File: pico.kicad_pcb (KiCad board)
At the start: 2 copper layers, 103 x 101.2 mm, 61 parts, among them J101 Programming, J102 ???, J103 XT60, J201 MR30, Q101 IRFS7434TRL7PP, Q201 SQJ142EP-T1_GE3, Q202 SQJ142EP-T1_GE3, Q203 SQJ142EP-T1_GE3, Q204 SQJ142EP-T1_GE3, Q205 SQJ142EP-T1_GE3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

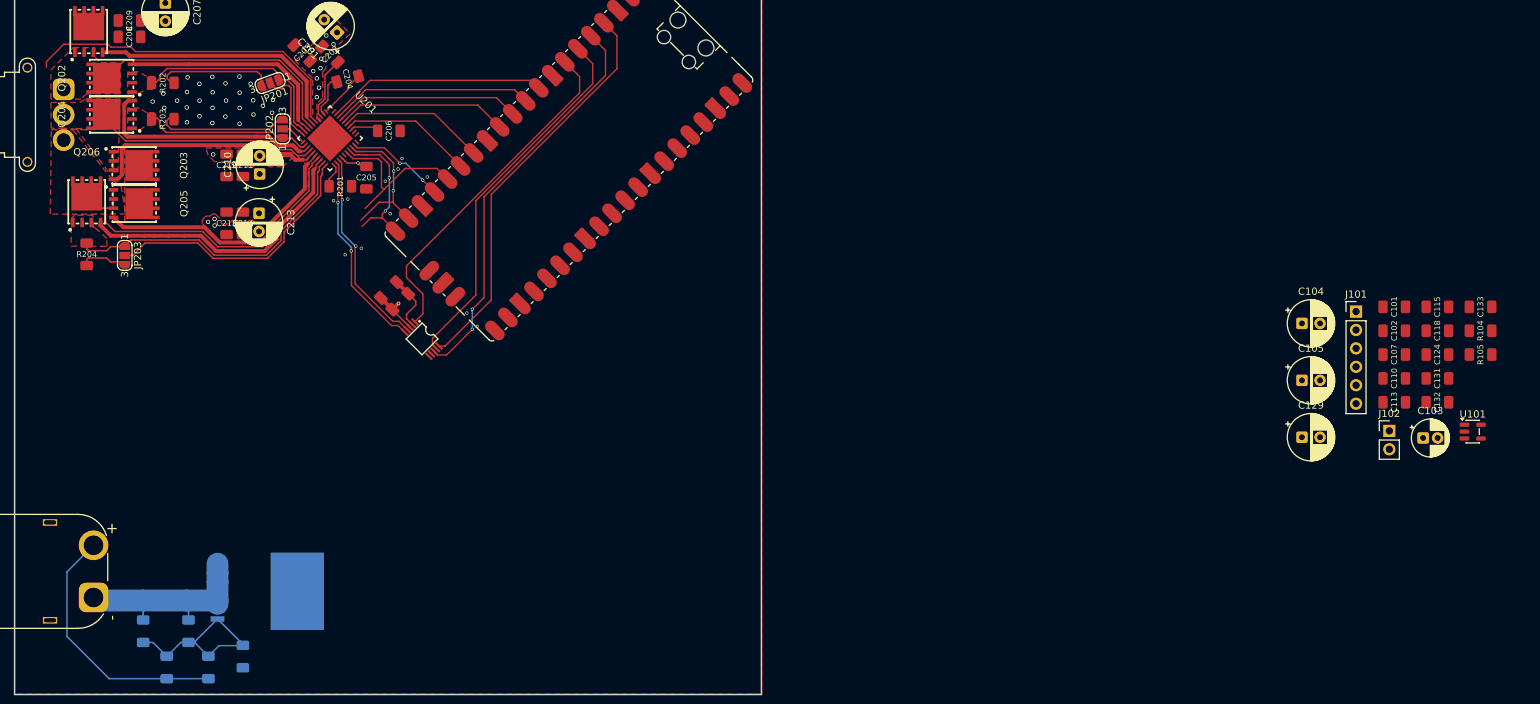
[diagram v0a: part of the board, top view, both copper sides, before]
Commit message: progress on pcb todo:encoders
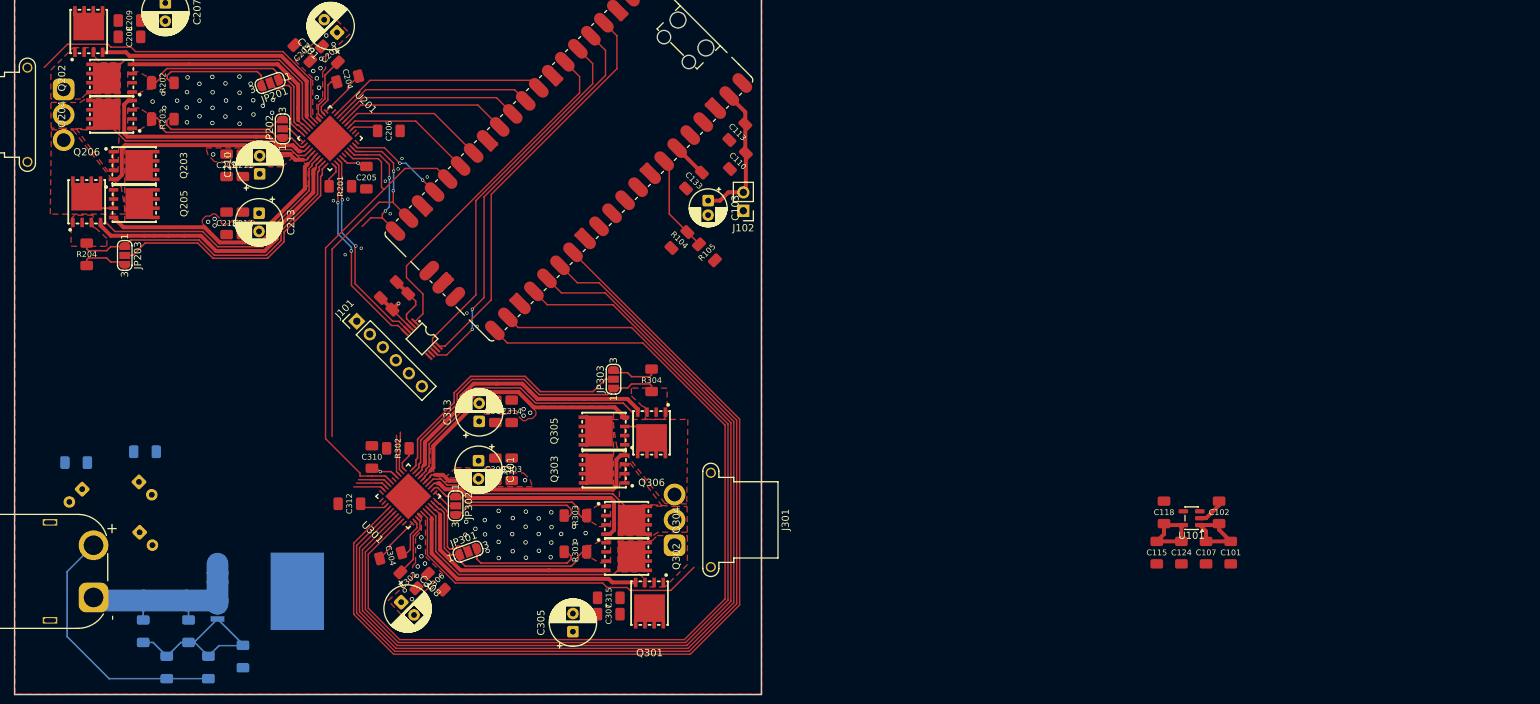
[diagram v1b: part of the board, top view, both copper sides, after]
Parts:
- added C301: 47u, Capacitor_THT:CP_Radial_D6.3mm_P2.50mm, F.Cu at (74.5, 129.2)
- added C302: 1u, COMPONENTS:1206_Resistor, F.Cu at (64.8, 145.7)
- added C303: 100n, COMPONENTS:1206_Resistor, F.Cu at (79.1, 130.4)
- added C304: 47n, COMPONENTS:1206_Resistor, F.Cu at (62.4, 142.3)
- added C305: 47u low ESR, Capacitor_THT:CP_Radial_D6.3mm_P2.50mm, F.Cu at (87.5, 152.8)
- added C306: 10u, COMPONENTS:1206_Resistor, F.Cu at (68.6, 145.9)
- added C307: 1u, COMPONENTS:1206_Resistor, F.Cu at (92.5, 150.4)
- added C308: 47u low ESR, Capacitor_THT:CP_Radial_D6.3mm_P2.50mm, F.Cu at (63.8, 148.7)
- added C309: 10u, COMPONENTS:1206_Resistor, F.Cu at (76.8, 130.4)
- added C310: 100n, COMPONENTS:1206_Resistor, F.Cu at (59.8, 128.7)
- added C311: 1u, COMPONENTS:1206_Resistor, F.Cu at (76.8, 122.4)
- added C312: 1u, COMPONENTS:1206_Resistor, F.Cu at (56.7, 135.2)
- added C313: 47u low ESR, Capacitor_THT:CP_Radial_D6.3mm_P2.50mm, F.Cu at (74.6, 123.8)
- added C314: 10u, COMPONENTS:1206_Resistor, F.Cu at (79.1, 122.4)
- added C315: 1u, COMPONENTS:1206_Resistor, F.Cu at (92.5, 148.2)
- added J301: MR30, Connector_AMASS:AMASS_MR30PW-FB_1x03_P3.50mm_Horizontal, F.Cu at (101.5, 140.9)
- added JP301: SolderJumper_3_Open, Jumper:SolderJumper-3_P1.3mm_Open_RoundedPad1.0x1.5mm_NumberLabels, F.Cu at (73.1, 141.8)
- added JP302: SolderJumper_3_Open, Jumper:SolderJumper-3_P1.3mm_Open_RoundedPad1.0x1.5mm_NumberLabels, F.Cu at (71.3, 135.5)
- added JP303: SolderJumper_3_Open, Jumper:SolderJumper-3_P1.3mm_Open_RoundedPad1.0x1.5mm_NumberLabels, F.Cu at (93.1, 118.0)
- added Q301: SQJ142EP-T1_GE3, JLCPCB_Transistors_Thyristors:POWERPAK-SO-8_L5.9-W4.9-P1.27-BL, F.Cu at (98.1, 148.9)
- added Q302: SQJ142EP-T1_GE3, JLCPCB_Transistors_Thyristors:POWERPAK-SO-8_L5.9-W4.9-P1.27-BL, F.Cu at (94.9, 142.4)
- added Q303: SQJ142EP-T1_GE3, JLCPCB_Transistors_Thyristors:POWERPAK-SO-8_L5.9-W4.9-P1.27-BL, F.Cu at (91.8, 130.4)
- added Q304: SQJ142EP-T1_GE3, JLCPCB_Transistors_Thyristors:POWERPAK-SO-8_L5.9-W4.9-P1.27-BL, F.Cu at (94.9, 137.4)
- added Q305: SQJ142EP-T1_GE3, JLCPCB_Transistors_Thyristors:POWERPAK-SO-8_L5.9-W4.9-P1.27-BL, F.Cu at (91.8, 125.1)
- added Q306: SQJ142EP-T1_GE3, JLCPCB_Transistors_Thyristors:POWERPAK-SO-8_L5.9-W4.9-P1.27-BL, F.Cu at (98.4, 125.4)
- added R301: 2m, COMPONENTS:1206_Resistor, F.Cu at (87.9, 141.8)
- added R302: 100k, COMPONENTS:1206_Resistor, F.Cu at (63.4, 127.5)
- added R303: 2m, COMPONENTS:1206_Resistor, F.Cu at (87.9, 136.8)
- added R304: 2m, COMPONENTS:1206_Resistor, F.Cu at (98.4, 118.2)
- added U301: DRV8323SRTAT, JLCPCB_Power_Supply_Chip:WQFN-40_L6.0-W6.0-P0.50-TL-EP4.5, F.Cu at (64.8, 134.1)
- C104, C105, C129, C131, C132: moved to B.Cu
- U101: value TPS7A2050PDBVR -> TPS7A2033PDBVR
- moved C132 187.9 mm to (19.0, 129.5), turned to 180 degrees
- moved C131 178.5 mm to (28.5, 128.0)
- moved C104 169.8 mm to (19.8, 133.2), turned to -135 degrees
- moved C105 161.0 mm to (27.7, 132.2), turned to -45 degrees
- moved C129 160.8 mm to (27.8, 139.1), turned to -45 degrees
- moved J101 137.8 mm to (57.7, 110.0), turned to 45 degrees
- moved R104 111.2 mm to (102.2, 98.8), turned to 45 degrees
- moved C133 109.9 mm to (104.2, 90.6), turned to -135 degrees
- moved R105 107.6 mm to (106.0, 100.5), turned to -45 degrees
- moved C103 103.9 mm to (106.2, 93.4), turned to -90 degrees
- moved C113 98.0 mm to (110.2, 83.9), turned to -135 degrees
- moved C110 95.4 mm to (110.3, 87.9), turned to -135 degrees
- moved J102 94.1 mm to (111.0, 94.8), turned to 180 degrees
- moved C115 51.4 mm to (168.0, 141.9), turned to -90 degrees
- moved C118 45.3 mm to (169.0, 136.4), turned to 90 degrees
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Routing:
- net PWM_B_X_H: track 0.00 -> 133.2 mm
- net PWM_B_X_L: track 0.00 -> 132.0 mm
- net PWM_B_Y_H: track 0.00 -> 130.9 mm
- net PWM_B_Y_L: track 0.00 -> 129.7 mm
- net PWM_B_Z_H: track 0.00 -> 129.6 mm
- net PWM_B_Z_L: track 0.00 -> 128.5 mm
- net /MotorDriver1/Z: track 0.00 -> 47.4 mm
- net GND: track 49.1 -> 95.2 mm, vias 50 -> 88
- net +BATT: track 82.4 -> 128.4 mm, vias 9 -> 18
- net SPI0_RX: track 23.6 -> 69.5 mm
- net /MotorDriver1/Z_S_H: track 0.00 -> 43.2 mm
- net /MotorDriver1/Z_L: track 0.00 -> 40.2 mm
- net /MotorDriver1/Z_S_L: track 0.00 -> 37.5 mm
- net /MotorDriver1/Z_H: track 0.00 -> 37.0 mm
- net /MotorDriver1/X_H: track 0.00 -> 36.1 mm
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- added copper zone on F.Cu, net /MotorDriver1/X
- added copper zone on F.Cu, net /MotorDriver1/X_S_H
- added copper zone on F.Cu, net /MotorDriver1/Y
- added copper zone on F.Cu, net /MotorDriver1/Y_S_H
- added copper zone on F.Cu, net /MotorDriver1/Z
- added copper zone on F.Cu, net /MotorDriver1/Z_S_H

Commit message: added m3 mounting holes
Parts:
- added H101: MountingHole, MountingHole:MountingHole_3.2mm_M3, F.Cu at (12.8, 62.5)
- added H102: MountingHole, MountingHole:MountingHole_3.2mm_M3, F.Cu at (111.3, 62.5)
- added H103: MountingHole, MountingHole:MountingHole_3.2mm_M3, F.Cu at (111.3, 159.3)
- added H104: MountingHole, MountingHole:MountingHole_3.2mm_M3, F.Cu at (12.8, 159.3)
- moved C118 51.6 mm to (125.2, 109.3)
- moved C101 51.6 mm to (134.4, 114.8)
- moved C107 51.6 mm to (131.0, 114.8)
- moved U101 51.6 mm to (129.0, 110.1)
- moved C115 51.6 mm to (124.2, 114.8)
- moved C124 51.6 mm to (127.6, 114.8)
- moved C102 51.6 mm to (132.8, 109.2)

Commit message: ewdwad
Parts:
- added J104: Conn_01x03, Connector_JST:JST_EH_B3B-EH-A_1x03_P2.50mm_Vertical, F.Cu at (83.5, 67.8)
- moved H104 3.36 mm to (15.0, 156.8)
- moved H103 2.66 mm to (109.5, 157.3)
- moved H101 2.47 mm to (14.5, 64.3)
- moved H102 2.47 mm to (109.5, 64.3)
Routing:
- net ENable: track 0.00 -> 30.5 mm
- net UartRX: track 0.00 -> 12.1 mm
- net UartTX: track 0.00 -> 11.9 mm
- net PWM_B_Z_L: track 128.5 -> 130.9 mm
- net PWM_B_Z_H: track 129.6 -> 132.1 mm
- net PWM_B_X_L: track 132.0 -> 134.5 mm
- net PWM_B_Y_L: track 129.7 -> 132.2 mm
- net PWM_B_Y_H: track 130.9 -> 133.3 mm
- net PWM_B_X_H: track 133.2 -> 135.6 mm

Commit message: wdawdawd
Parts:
- moved J101 17.2 mm to (46.6, 123.1), turned to 180 degrees
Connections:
- U106 pad 6: ADC2+ -> ADC3+
- U106 pad 7: ADC3+ -> ADC2+
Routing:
- net SPI0_TX: track 24.5 -> 61.6 mm
- net SPI0_RX: track 69.5 -> 34.4 mm
- net CS_ENCODER_A: track 0.00 -> 22.7 mm, vias 0 -> 1
- net CS_ENCODER_B: track 0.00 -> 20.6 mm, vias 0 -> 1
- net CS_DRV_B: track 4.78 -> 20.0 mm, vias 0 -> 1
- net SPI0_CLK: track 56.5 -> 64.3 mm
- net ADC3+: track 5.57 -> 4.05 mm
- net ADC2+: track 5.69 -> 4.36 mm
- net SPI1_CS: track 48.0 -> 48.9 mm
- net PWM_B_X_H: track 135.6 -> 136.1 mm

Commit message: why every commit needs a message
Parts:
- added Q102: BSS138, Package_TO_SOT_SMD:SOT-23, F.Cu at (34.3, 112.8)
- added R102: 100, COMPONENTS:1206_Resistor, F.Cu at (34.8, 108.9)
- moved C305 0.34 mm to (87.5, 152.5)
- moved C214 0.13 mm to (42.0, 96.4)
- moved C215 0.12 mm to (39.8, 96.4)
- moved C314 0.06 mm to (79.1, 122.5)
- moved C311 0.06 mm to (76.8, 122.5)
- moved C313 0.05 mm to (74.6, 123.8)
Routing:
- net PWM_B_Z_L: track 130.9 -> 132.2 mm
- net PWM_B_Z_H: track 132.2 -> 133.4 mm
- net PWM_B_Y_L: track 132.4 -> 133.6 mm
- net PWM_B_X_L: track 134.9 -> 136.1 mm
- net PWM_B_Y_H: track 133.6 -> 134.9 mm
- net PWM_B_X_H: track 136.1 -> 137.4 mm

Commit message: Good progress
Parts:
- removed C117: 1u, COMPONENTS:1206_Resistor
- removed C122: DNP, COMPONENTS:1206_Resistor
- removed C123: 100n, COMPONENTS:1206_Resistor
- removed J201, J301: MR30, Connector_AMASS:AMASS_MR30PW-FB_1x03_P3.50mm_Horizontal
- removed R114: 2Meg, COMPONENTS:1206_Resistor
- added C106: 2200u, Capacitor_THT:CP_Radial_D18.0mm_P7.50mm, F.Cu at (47.0, 140.5)
- added H201: MountingHole_Pad, Connector_Wire:SolderWire-2sqmm_1x01_D2mm_OD3.9mm, F.Cu at (14.5, 75.3)
- added H202: MountingHole_Pad, Connector_Wire:SolderWire-2sqmm_1x01_D2mm_OD3.9mm, F.Cu at (14.5, 83.3)
- added H203: MountingHole_Pad, Connector_Wire:SolderWire-2sqmm_1x01_D2mm_OD3.9mm, F.Cu at (14.5, 91.8)
- added H301: MountingHole_Pad, Connector_Wire:SolderWire-2sqmm_1x01_D2mm_OD3.9mm, F.Cu at (104.8, 143.0)
- added H302: MountingHole_Pad, Connector_Wire:SolderWire-2sqmm_1x01_D2mm_OD3.9mm, F.Cu at (104.8, 135.3)
- added H303: MountingHole_Pad, Connector_Wire:SolderWire-2sqmm_1x01_D2mm_OD3.9mm, F.Cu at (104.8, 127.3)
- added Q103: AGM30P100D, EasyEDA_Lib:TO-252-3_L6.6-W6.1-P4.57-LS9.9-BR-CW, B.Cu at (34.3, 133.0)
- added Q104: AGM30P100D, EasyEDA_Lib:TO-252-3_L6.6-W6.1-P4.57-LS9.9-BR-CW, B.Cu at (34.3, 125.8)
- added Q105: AGM30P100D, EasyEDA_Lib:TO-252-3_L6.6-W6.1-P4.57-LS9.9-BR-CW, B.Cu at (34.3, 118.5)
- added Q106: AGM30P100D, EasyEDA_Lib:TO-252-3_L6.6-W6.1-P4.57-LS9.9-BR-CW, B.Cu at (34.3, 111.3)
- added R103: 100, COMPONENTS:1206_Resistor, B.Cu at (39.3, 148.3)
- added R106: 100, COMPONENTS:1206_Resistor, B.Cu at (36.8, 148.3)
- added R107: 100, COMPONENTS:1206_Resistor, B.Cu at (34.0, 148.3)
- added R108: 5k, COMPONENTS:1206_Resistor, F.Cu at (24.8, 116.3)
- C104, C105, C129: moved to F.Cu
- Q101: value IRFS7434TRL7PP -> AGM30P100D; footprint JLCPCB_Transistors:D2PAK-7_L10.6-W9.6-P1.27-LS15.9-BR -> EasyEDA_Lib:TO-252-3_L6.6-W6.1-P4.57-LS9.9-BR-CW
- R101: value 100k -> 100
- R102: moved to B.Cu
- moved J101 120.9 mm to (162.0, 87.2)
- moved C124 70.0 mm to (71.8, 72.4)
- moved C115 70.0 mm to (68.4, 72.4)
- moved C102 70.0 mm to (77.0, 66.9)
- moved U101 70.0 mm to (73.2, 67.7)
- moved C118 70.0 mm to (69.4, 66.9)
- moved C107 70.0 mm to (75.2, 72.4)
- moved C101 70.0 mm to (78.6, 72.4)
- moved C104 40.0 mm to (-20.2, 133.2), turned to -45 degrees
- moved C105 40.0 mm to (-12.4, 132.2), turned to -135 degrees
- moved C129 40.0 mm to (-12.3, 139.1), turned to -135 degrees
- moved C131 40.0 mm to (-11.5, 128.0)
- moved C132 40.0 mm to (-21.0, 129.5)
- moved R102 40.0 mm to (41.8, 148.3), turned to 90 degrees
- moved J103 18.4 mm to (21.4, 129.7)
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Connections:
- J103 pad 1: Net-(J103-Pin_1) -> GND
- J103 pad 2: +BATT -> /IN
- Q101 pad 2: Net-(J103-Pin_1) -> +BATT
- Q101 pad 3: Net-(J103-Pin_1) -> /IN
- Q102 pad 1: ENableBATT -> ENable
- Q102 pad 2: Net-(Q101-G) -> GND
- Q102 pad 3: +BATT -> Net-(Q101-G)
- R101 pad 1: +BATT -> /IN
- R101 pad 2: Net-(Q101-G) -> +BATT
- R102 pad 1: Net-(J103-Pin_1) -> /IN
- R102 pad 2: GND -> +BATT
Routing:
- net +LDO: track 32.0 -> 144.2 mm, vias 2 -> 7
- net +BATT: track 128.4 -> 37.5 mm
- net ENable: track 30.8 -> 74.3 mm, vias 0 -> 2
- net +5VP: track 31.6 -> 70.3 mm, vias 0 -> 2
- net /IN: track 0.00 -> 31.3 mm
- net Net-(J103-Pin_1): track 28.3 -> 0.00 mm
- net Net-(Q101-G): track 27.1 -> 44.7 mm, vias 0 -> 5
- net SPI0_RX: track 34.0 -> 21.4 mm
- net Net-(U201-CPL): track 6.72 -> 8.79 mm
- net GND: track 95.2 -> 95.8 mm, vias 88 -> 135
- added copper zone on F.Cu, net +5VP
- added copper zone on B.Cu, net +BATT
- added copper zone on F.Cu, net +LDO
- added copper zone on B.Cu, net /IN

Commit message: done?
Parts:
- removed C103: 22u, Capacitor_THT:CP_Radial_D5.0mm_P2.00mm
- removed C131: 10u, COMPONENTS:1206_Resistor
- removed C132: 1u, COMPONENTS:1206_Resistor
- removed H101, H102, H103, H104: MountingHole, MountingHole:MountingHole_3.2mm_M3
- removed J102: ???, Connector_PinHeader_2.54mm:PinHeader_1x02_P2.54mm_Vertical
- added H105: MountingHole_Pad, MountingHole:MountingHole_3.2mm_M3_Pad_Via, F.Cu at (14.5, 64.3)
- added H106: MountingHole_Pad, MountingHole:MountingHole_3.2mm_M3_Pad_Via, F.Cu at (109.5, 64.3)
- added H107: MountingHole_Pad, MountingHole:MountingHole_3.2mm_M3_Pad_Via, F.Cu at (109.5, 157.4)
- added H108: MountingHole_Pad, MountingHole:MountingHole_3.2mm_M3_Pad_Via, F.Cu at (14.5, 157.4)
- added J105: Conn_01x03, Connector_JST:JST_XH_B3B-XH-A_1x03_P2.50mm_Vertical, F.Cu at (101.8, 95.7)
- added J106: Conn_01x03, Connector_JST:JST_XH_B3B-XH-A_1x03_P2.50mm_Vertical, F.Cu at (56.2, 110.4)
- added J107: Conn_01x03, Connector_JST:JST_XH_B3B-XH-A_1x03_P2.50mm_Vertical, F.Cu at (95.8, 101.7)
- added J108: Conn_01x03, Connector_JST:JST_XH_B3B-XH-A_1x03_P2.50mm_Vertical, F.Cu at (55.6, 119.7)
- added JP101: SolderJumper_2_Open, Jumper:SolderJumper-2_P1.3mm_Open_RoundedPad1.0x1.5mm, F.Cu at (102.1, 63.1)
- J101: value Programming -> Conn_01x03; footprint Connector_PinHeader_2.54mm:PinHeader_1x06_P2.54mm_Vertical -> Connector_JST:JST_XH_B3B-XH-A_1x03_P2.50mm_Vertical
- J104: footprint Connector_JST:JST_EH_B3B-EH-A_1x03_P2.50mm_Vertical -> Connector_JST:JST_XH_B3B-XH-A_1x03_P2.50mm_Vertical
- moved J101 99.7 mm to (64.1, 68.7), turned to 90 degrees
- moved C104 62.1 mm to (34.1, 103.1), turned to 180 degrees
- moved C129 60.6 mm to (47.7, 130.5), turned to 135 degrees
- moved C105 59.4 mm to (46.4, 123.4), turned to 90 degrees
- moved C101 9.83 mm to (76.6, 62.8), turned to 0 degrees
- moved R104 9.32 mm to (110.9, 95.5), turned to 90 degrees
- moved R105 8.41 mm to (108.4, 92.4), turned to 90 degrees
- moved C115 8.24 mm to (76.6, 73.0), turned to 0 degrees
- moved C102 6.43 mm to (71.1, 64.4), turned to 180 degrees
- moved C107 6.38 mm to (76.6, 66.2), turned to 0 degrees
- moved C124 5.59 mm to (76.6, 69.6), turned to 0 degrees
- moved C118 5.39 mm to (71.1, 72.0), turned to 180 degrees
- moved C133 3.10 mm to (106.4, 88.4), turned to 45 degrees
- moved C208 2.25 mm to (27.8, 69.5)
- moved C209 2.25 mm to (30.0, 69.5)
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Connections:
- A101 pad 37: ENable -> Net-(A101-3V3_EN)
- J101 pad 2: +5VP -> unconnected-(J101-Pin_2-Pad2)
- J101 pad 3: SWCLK -> +5VP
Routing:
- net ENable: track 74.3 -> 156.1 mm, vias 2 -> 7
- net CS_DRV_B: track 20.0 -> 74.0 mm, vias 1 -> 2
- net SPI0_RX: track 21.4 -> 71.6 mm, vias 0 -> 2
- net Net-(A101-3V3_EN): track 0.00 -> 24.5 mm
- net +BATT: track 37.5 -> 62.0 mm, vias 18 -> 139
- net ADC3+: track 4.05 -> 19.7 mm
- net CS_ENCODER_A: track 22.7 -> 7.02 mm, vias 1 -> 0
- net ADC2+: track 4.36 -> 19.7 mm
- net +LDO: track 144.2 -> 159.5 mm
- net CS_ENCODER_B: track 20.6 -> 8.81 mm, vias 1 -> 0
- net VbatADC: track 13.5 -> 21.2 mm
- net +5VP: track 70.3 -> 74.9 mm
- net SPI0_CLK: track 64.3 -> 68.2 mm, vias 2 -> 0
- net SPI0_TX: track 62.0 -> 60.2 mm
- net PWM_A_X_H: track 18.3 -> 19.2 mm
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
